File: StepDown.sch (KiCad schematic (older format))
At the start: 18 parts, among them J604 Conn_02x01, J605 Conn_02x01, Q1 2N7002, U602 TPS560430

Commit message: Änderungen von der Arbeit, Viele LCSC Teile für teurere ausgetauscht
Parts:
- removed R_FBB601: 20K, Resistor_SMD:R_0603_1608Metric_Pad1.05x0.95mm_HandSolder, symbol Device:R_Small
- added R601: 3K3, Resistor_SMD:R_0603_1608Metric_Pad1.05x0.95mm_HandSolder, symbol Device:R_Small
- R_FBT601: value 47K -> 10K
- U602: value TPS560430 -> JW5026
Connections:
- net GND: now also R601.1
- net at R_FBT601.1, U602.3 (FB): now also R601.2
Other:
- note added: "3K3"
- note added: "JW5026 / TPS560430\n2K4/3K3 = R_FBB601\n7K5/10K = R_FBT601"
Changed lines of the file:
@@
 P 5950 3150
 F 0 "U602" H 5950 3475 50  0000 C CNN
-F 1 "TPS560430" H 5950 3384 50  0000 C CNN
+F 1 "JW5026" H 5950 3384 50  0000 C CNN
 F 2 "Package_TO_SOT_SMD:SOT-23-6_Handsoldering" H 5150 2750 50  0001 L CNN
 F 3 "https://www.ti.com/lit/ds/symlink/tps560430.pdf?ts=1590476433528" H 5700 2800 50  0001 C CNN
@@
 AR Path="/5ED2496F/5ECED53D" Ref="R_FBT601"  Part="1"
 F 0 "R_FBT601" H 7050 3400 50  0000 C CNN
-F 1 "47K" H 7050 3300 50  0000 C CNN
+F 1 "10K" H 7050 3300 50  0000 C CNN
 F 2 "Resistor_SMD:R_0603_1608Metric_Pad1.05x0.95mm_HandSolder" H 7250 3300 50  0001 C CNN
 F 3 "~" H 7250 3300 50  0001 C CNN
@@
 	-1   0    0    1
 $EndComp
-$Comp
-L Device:R_Small R?
-U 1 1 5ECED695
-P 7250 3600
-AR Path="/5ECED695" Ref="R?"  Part="1"
-AR Path="/5ED2496F/5ECED695" Ref="R_FBB601"  Part="1"
-F 0 "R_FBB601" H 7050 3700 50  0000 C CNN
-F 1 "20K" H 7050 3600 50  0000 C CNN
-F 2 "Resistor_SMD:R_0603_1608Metric_Pad1.05x0.95mm_HandSolder" H 7250 3600 50  0001 C CNN
-F 3 "~" H 7250 3600 50  0001 C CNN
-	1    7250 3600
-	-1   0    0    1
-$EndComp
 Wire Wire Line
 	7250 3400 7250 3450
@@
 L power:GND #PWR0125
 U 1 1 5ECEED06
-P 7250 3700
-F 0 "#PWR0125" H 7250 3450 50  0001 C CNN
-F 1 "GND" H 7255 3527 50  0000 C CNN
-F 2 "" H 7250 3700 50  0001 C CNN
-F 3 "" H 7250 3700 50  0001 C CNN
-	1    7250 3700
+P 7250 3850
+F 0 "#PWR0125" H 7250 3600 50  0001 C CNN
+F 1 "GND" H 7255 3677 50  0000 C CNN
+F 2 "" H 7250 3850 50  0001 C CNN
+F 3 "" H 7250 3850 50  0001 C CNN
+	1    7250 3850
 	1    0    0    -1
 $EndComp
@@
 Text Notes 7050 3350 0    50   ~ 0
 51K
-Text Notes 7000 3650 0    50   ~ 0
+Text Notes 6750 3550 0    50   ~ 0
 22K1
+Text Notes 6150 3900 0    50   ~ 0
+JW5026 / TPS560430\n2K4/3K3 = R_FBB601\n7K5/10K = R_FBT601
+Text Notes 7300 3800 0    50   ~ 0
+3K3
+$Comp
+L Device:R_Small R?
+U 1 1 5EF8D983
+P 7250 3600
+AR Path="/5EF8D983" Ref="R?"  Part="1"
+AR Path="/5ED2496F/5EF8D983" Ref="R601"  Part="1"
+F 0 "R601" H 7100 3550 50  0000 C CNN
+F 1 "3K3" H 7100 3650 50  0000 C CNN
+F 2 "Resistor_SMD:R_0603_1608Metric_Pad1.05x0.95mm_HandSolder" H 7250 3600 50  0001 C CNN
+F 3 "~" H 7250 3600 50  0001 C CNN
+	1    7250 3600
+	-1   0    0    1
+$EndComp
+Wire Wire Line
+	7250 3700 7250 3850
 $EndSCHEMATC

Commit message: Fast fertig TODO: Connector umverdrahten mit beschriftung
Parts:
- C601: value 2.2u -> 10u; footprint Capacitor_THT:CP_Radial_D6.3mm_P2.50mm -> Capacitor_THT:CP_Radial_D4.0mm_P2.00mm
- C602, C607, C608: value 100nF -> 100n
- C611: value 22u -> 10u; footprint Capacitor_THT:CP_Radial_D6.3mm_P2.50mm -> Capacitor_THT:CP_Radial_D4.0mm_P2.00mm
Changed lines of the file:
@@
 AR Path="/5ED2496F/5ECEAD6C" Ref="C608"  Part="1"
 F 0 "C608" V 6200 3000 50  0000 L CNN
-F 1 "100nF" V 6300 2950 50  0000 L CNN
+F 1 "100n" V 6300 2950 50  0000 L CNN
 F 2 "Capacitor_SMD:C_0603_1608Metric_Pad1.05x0.95mm_HandSolder" H 6450 3050 50  0001 C CNN
 F 3 "~" H 6450 3050 50  0001 C CNN
@@
 AR Path="/5ED2496F/5ECF3151" Ref="C611"  Part="1"
 F 0 "C611" H 7791 3496 50  0000 L CNN
-F 1 "22u" H 7791 3405 50  0000 L CNN
-F 2 "Capacitor_THT:CP_Radial_D6.3mm_P2.50mm" H 7700 3450 50  0001 C CNN
+F 1 "10u" H 7791 3405 50  0000 L CNN
+F 2 "Capacitor_THT:CP_Radial_D4.0mm_P2.00mm" H 7700 3450 50  0001 C CNN
 F 3 "~" H 7700 3450 50  0001 C CNN
 	1    7700 3450
@@
 AR Path="/5ED2496F/5ECF706C" Ref="C601"  Part="1"
 F 0 "C601" H 3991 3296 50  0000 L CNN
-F 1 "2.2u" H 3991 3205 50  0000 L CNN
-F 2 "Capacitor_THT:CP_Radial_D6.3mm_P2.50mm" H 3900 3250 50  0001 C CNN
+F 1 "10u" H 3991 3205 50  0000 L CNN
+F 2 "Capacitor_THT:CP_Radial_D4.0mm_P2.00mm" H 3900 3250 50  0001 C CNN
 F 3 "~" H 3900 3250 50  0001 C CNN
 	1    3900 3250
@@
 AR Path="/5ED2496F/5ECF71D3" Ref="C602"  Part="1"
 F 0 "C602" H 4000 3200 50  0000 L CNN
-F 1 "100nF" H 3850 3300 50  0000 L CNN
+F 1 "100n" H 3850 3300 50  0000 L CNN
 F 2 "Capacitor_SMD:C_0603_1608Metric_Pad1.05x0.95mm_HandSolder" H 4200 3250 50  0001 C CNN
 F 3 "~" H 4200 3250 50  0001 C CNN
@@
 AR Path="/5ED2496F/5ED1796C" Ref="C607"  Part="1"
 F 0 "C607" H 5250 3500 50  0000 L CNN
-F 1 "100nF" H 5150 3600 50  0000 L CNN
+F 1 "100n" H 5150 3600 50  0000 L CNN
 F 2 "Capacitor_SMD:C_0603_1608Metric_Pad1.05x0.95mm_HandSolder" H 5050 3550 50  0001 C CNN
 F 3 "~" H 5050 3550 50  0001 C CNN

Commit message: Bereit zur Bestellung
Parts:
- C601, C611: footprint Capacitor_THT:CP_Radial_D4.0mm_P2.00mm -> Capacitor_SMD:C_1206_3216Metric_Pad1.42x1.75mm_HandSolder; symbol Device:CP1_Small -> Device:C_Small
- U602: symbol MukkeBox-rescue:TPS560430-Regulator_Switching -> MukkeBox-rescue:TPS560430-Regulator_Switching-MukkeBox-rescue
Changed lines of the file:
@@
 EESchema Schematic File Version 4
-LIBS:MukkeBox-cache
-EELAYER 26 0
+EELAYER 30 0
 EELAYER END
 $Descr A4 11693 8268
@@
 	9000 3200 8250 3200
 $Comp
-L MukkeBox-rescue:TPS560430-Regulator_Switching U602
+L MukkeBox-rescue:TPS560430-Regulator_Switching-MukkeBox-rescue U602
 U 1 1 5ECDAABE
 P 5950 3150
@@
 	5550 3350 5550 3750
 $Comp
-L Device:CP1_Small C?
+L Device:C_Small C?
 U 1 1 5ECF3151
 P 7700 3450
@@
 F 0 "C611" H 7791 3496 50  0000 L CNN
 F 1 "10u" H 7791 3405 50  0000 L CNN
-F 2 "Capacitor_THT:CP_Radial_D4.0mm_P2.00mm" H 7700 3450 50  0001 C CNN
+F 2 "Capacitor_SMD:C_1206_3216Metric_Pad1.42x1.75mm_HandSolder" H 7700 3450 50  0001 C CNN
 F 3 "~" H 7700 3450 50  0001 C CNN
 	1    7700 3450
@@
 $EndComp
 $Comp
-L Device:CP1_Small C?
+L Device:C_Small C?
 U 1 1 5ECF706C
 P 3900 3250
@@
 F 0 "C601" H 3991 3296 50  0000 L CNN
 F 1 "10u" H 3991 3205 50  0000 L CNN
-F 2 "Capacitor_THT:CP_Radial_D4.0mm_P2.00mm" H 3900 3250 50  0001 C CNN
+F 2 "Capacitor_SMD:C_1206_3216Metric_Pad1.42x1.75mm_HandSolder" H 3900 3250 50  0001 C CNN
 F 3 "~" H 3900 3250 50  0001 C CNN
 	1    3900 3250

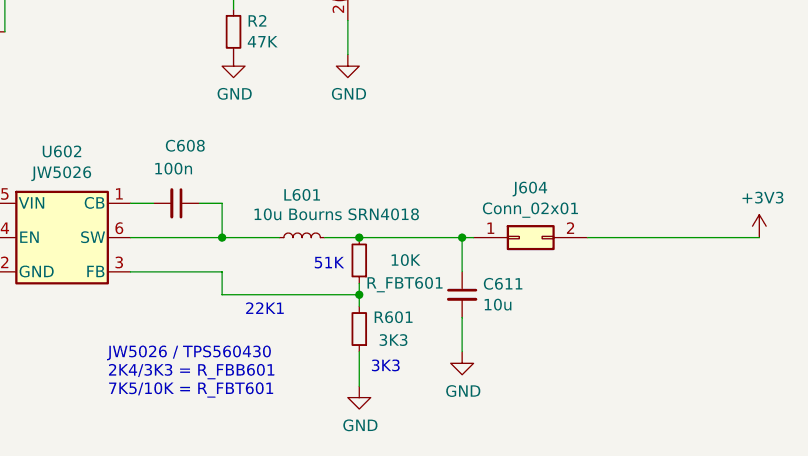
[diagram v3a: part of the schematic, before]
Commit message: I2C Dreher behoben, BOM vereinfacht, 20dB Gain an ClassD Amps
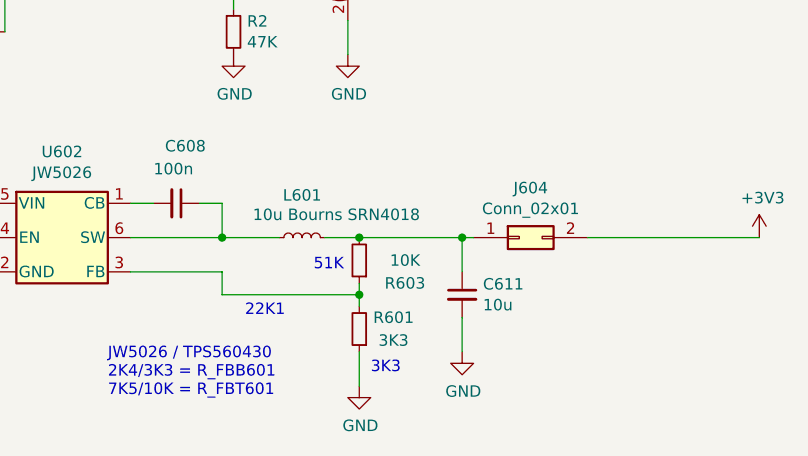
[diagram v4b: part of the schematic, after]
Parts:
- renumbered R_FBT601 to R603
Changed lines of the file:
@@
 EESchema Schematic File Version 4
-EELAYER 30 0
+LIBS:MukkeBox-cache
+EELAYER 26 0
 EELAYER END
 $Descr A4 11693 8268
@@
 P 7250 3300
 AR Path="/5ECED53D" Ref="R?"  Part="1"
-AR Path="/5ED2496F/5ECED53D" Ref="R_FBT601"  Part="1"
-F 0 "R_FBT601" H 7050 3400 50  0000 C CNN
+AR Path="/5ED2496F/5ECED53D" Ref="R603"  Part="1"
+F 0 "R603" H 7050 3400 50  0000 C CNN
 F 1 "10K" H 7050 3300 50  0000 C CNN
 F 2 "Resistor_SMD:R_0603_1608Metric_Pad1.05x0.95mm_HandSolder" H 7250 3300 50  0001 C CNN
